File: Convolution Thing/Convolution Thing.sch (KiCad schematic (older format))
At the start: 4 parts, among them U1 Compute_Module_4_Functional

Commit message: Just EE things
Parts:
- removed U1: Compute_Module_4_Functional, CM4:Raspberry-Pi-4-Compute-Module, symbol CM4:Compute_Module_4_Functional
- removed U? (x3): Compute_Module_4_Functional, symbol CM4:Compute_Module_4_Functional
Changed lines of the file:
@@
 $Descr A4 11693 8268
 encoding utf-8
-Sheet 1 2
+Sheet 1 4
 Title ""
 Date ""
@@
 Comment4 ""
 $EndDescr
-$Comp
-L CM4:Compute_Module_4_Functional U1
-U 1 1 6100CB94
-P 1100 1150
-F 0 "U1" H 1950 1447 60  0000 C CNN
-F 1 "Compute_Module_4_Functional" H 1950 1341 60  0000 C CNN
-F 2 "CM4:Raspberry-Pi-4-Compute-Module" H 1300 1200 60  0001 L CNN
-F 3 "" H 1300 1000 60  0001 L CNN
-	1    1100 1150
-	1    0    0    -1
-$EndComp
-$Comp
-L CM4:Compute_Module_4_Functional U?
-U 2 1 61012F62
-P 3700 2200
-F 0 "U?" H 4400 2487 60  0000 C CNN
-F 1 "Compute_Module_4_Functional" H 4400 2381 60  0000 C CNN
-F 2 "" H 3900 2250 60  0001 L CNN
-F 3 "" H 3900 2050 60  0001 L CNN
-	2    3700 2200
-	1    0    0    -1
-$EndComp
-$Comp
-L CM4:Compute_Module_4_Functional U?
-U 8 1 61015F4E
-P 1500 2450
-F 0 "U?" H 2108 2737 60  0000 C CNN
-F 1 "Compute_Module_4_Functional" H 2108 2631 60  0000 C CNN
-F 2 "" H 1700 2500 60  0001 L CNN
-F 3 "" H 1700 2300 60  0001 L CNN
-	8    1500 2450
-	1    0    0    -1
-$EndComp
-$Comp
-L CM4:Compute_Module_4_Functional U?
-U 10 1 61019A69
-P 5850 1200
-F 0 "U?" H 6800 1487 60  0000 C CNN
-F 1 "Compute_Module_4_Functional" H 6800 1381 60  0000 C CNN
-F 2 "" H 6050 1250 60  0001 L CNN
-F 3 "" H 6050 1050 60  0001 L CNN
-	10   5850 1200
-	1    0    0    -1
-$EndComp
 $Sheet
-S 2700 5250 800  750
+S 1750 850  800  750
+U 61029798
+F0 "CODEC" 50
+F1 "CODEC.sch" 50
+$EndSheet
+$Sheet
+S 800  850  800  750
 U 61006232
 F0 "PSU" 50
 F1 "PSU.sch" 50
 $EndSheet
+$Sheet
+S 2700 850  850  750
+U 6108AFC4
+F0 "Misc" 50
+F1 "Misc.sch" 50
+$EndSheet
 $EndSCHEMATC

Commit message: Convolution Thing PCB design continues
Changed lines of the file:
@@
 $Descr A4 11693 8268
 encoding utf-8
-Sheet 1 4
+Sheet 1 7
 Title ""
 Date ""
@@
 S 2700 850  850  750
 U 6108AFC4
-F0 "Misc" 50
-F1 "Misc.sch" 50
+F0 "CM4 Misc" 50
+F1 "CM4 Misc.sch" 50
+$EndSheet
+$Sheet
+S 3700 850  850  750
+U 610884FE
+F0 "CM4 GPIO" 50
+F1 "CM4 GPIO.sch" 50
+$EndSheet
+$Sheet
+S 5700 850  850  750
+U 610554DD
+F0 "Audio Out" 50
+F1 "Audio Out.sch" 50
+$EndSheet
+$Sheet
+S 4700 850  850  750
+U 61055545
+F0 "Audio In" 50
+F1 "Audio In.sch" 50
 $EndSheet
 $EndSCHEMATC

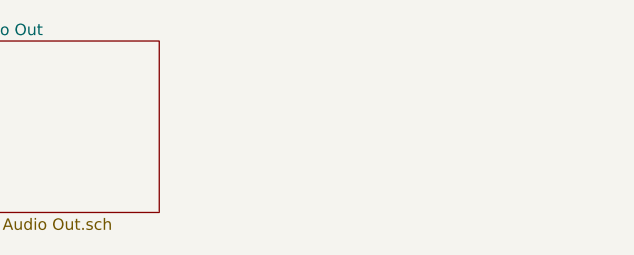
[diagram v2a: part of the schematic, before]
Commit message: Audio I/O, CV input, GPIO work & misc changes
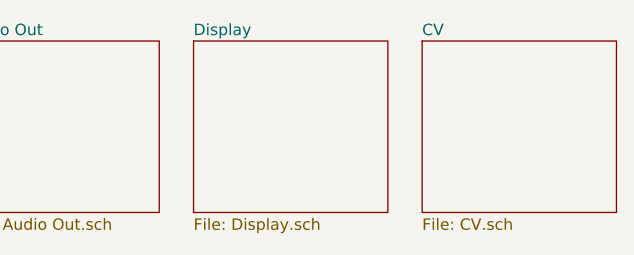
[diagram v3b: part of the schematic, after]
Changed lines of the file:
@@
 $Descr A4 11693 8268
 encoding utf-8
-Sheet 1 7
+Sheet 1 9
 Title ""
 Date ""
@@
 F1 "Audio In.sch" 50
 $EndSheet
+$Sheet
+S 6700 850  850  750
+U 6110E798
+F0 "Display" 50
+F1 "Display.sch" 50
+$EndSheet
+$Sheet
+S 7700 850  850  750
+U 611124FC
+F0 "CV" 50
+F1 "CV.sch" 50
+$EndSheet
 $EndSCHEMATC

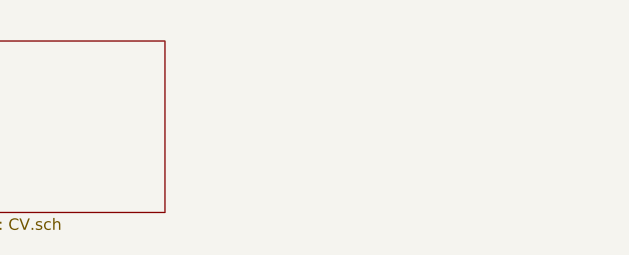
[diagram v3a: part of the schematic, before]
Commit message: Better CV inputs, LED driver, display & USB interfaces
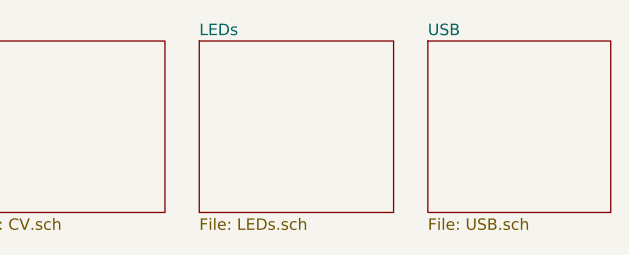
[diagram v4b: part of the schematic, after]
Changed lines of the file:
@@
 $Descr A4 11693 8268
 encoding utf-8
-Sheet 1 9
+Sheet 1 11
 Title ""
 Date ""
@@
 F1 "CV.sch" 50
 $EndSheet
+$Sheet
+S 8700 850  850  750
+U 611DE4E7
+F0 "LEDs" 50
+F1 "LEDs.sch" 50
+$EndSheet
+$Sheet
+S 9700 850  800  750
+U 61201209
+F0 "USB" 50
+F1 "USB.sch" 50
+$EndSheet
 $EndSCHEMATC

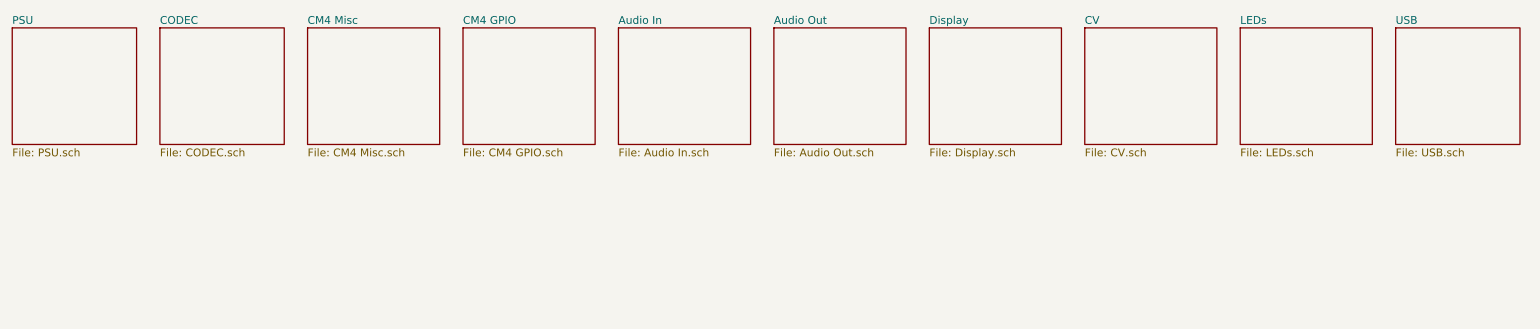
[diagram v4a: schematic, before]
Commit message: Added gate inputs and CM4 / display sockets, made CV inputs 100k, lots of smaller changes. First iteration of schematic now done.
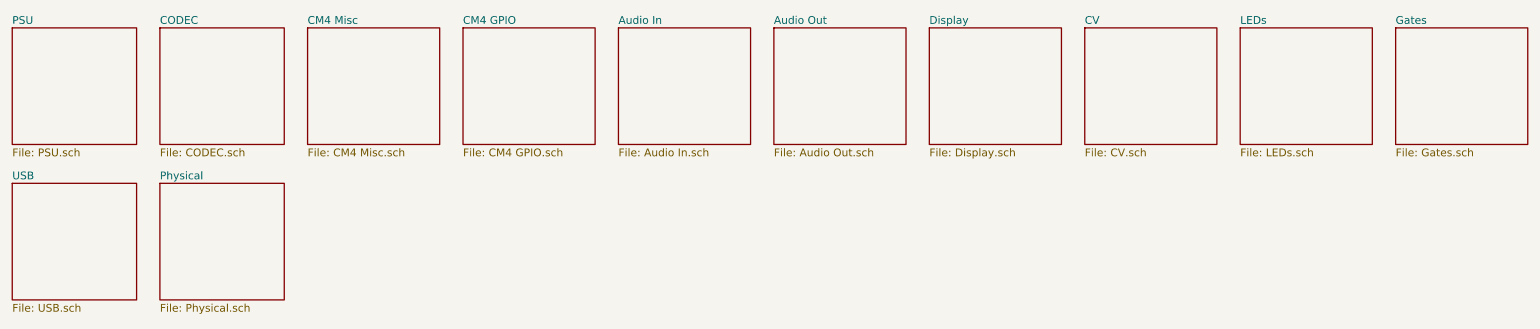
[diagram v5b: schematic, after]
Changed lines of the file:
@@
 $Descr A4 11693 8268
 encoding utf-8
-Sheet 1 11
+Sheet 1 13
 Title ""
 Date ""
@@
 $EndSheet
 $Sheet
-S 9700 850  800  750
+S 800  1850 800  750
 U 61201209
 F0 "USB" 50
 F1 "USB.sch" 50
 $EndSheet
+$Sheet
+S 9700 850  850  750
+U 610C04CE
+F0 "Gates" 50
+F1 "Gates.sch" 50
+$EndSheet
+$Sheet
+S 1750 1850 800  750
+U 610E9296
+F0 "Physical" 50
+F1 "Physical.sch" 50
+$EndSheet
 $EndSCHEMATC

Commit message: PCB layout work and related changes to the schematic
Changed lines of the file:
@@
 $EndDescr
 $Sheet
-S 1750 850  800  750
+S 2700 850  850  750
 U 61029798
 F0 "CODEC" 50
@@
 $EndSheet
 $Sheet
-S 2700 850  850  750
-U 6108AFC4
-F0 "CM4 Misc" 50
-F1 "CM4 Misc.sch" 50
-$EndSheet
-$Sheet
 S 3700 850  850  750
 U 610884FE
-F0 "CM4 GPIO" 50
-F1 "CM4 GPIO.sch" 50
+F0 "GPIO" 50
+F1 "GPIO.sch" 50
 $EndSheet
 $Sheet
@@
 F1 "Physical.sch" 50
 $EndSheet
+$Sheet
+S 1750 850  850  750
+U 6121D935
+F0 "CM4" 50
+F1 "CM4.sch" 50
+$EndSheet
 $EndSCHEMATC

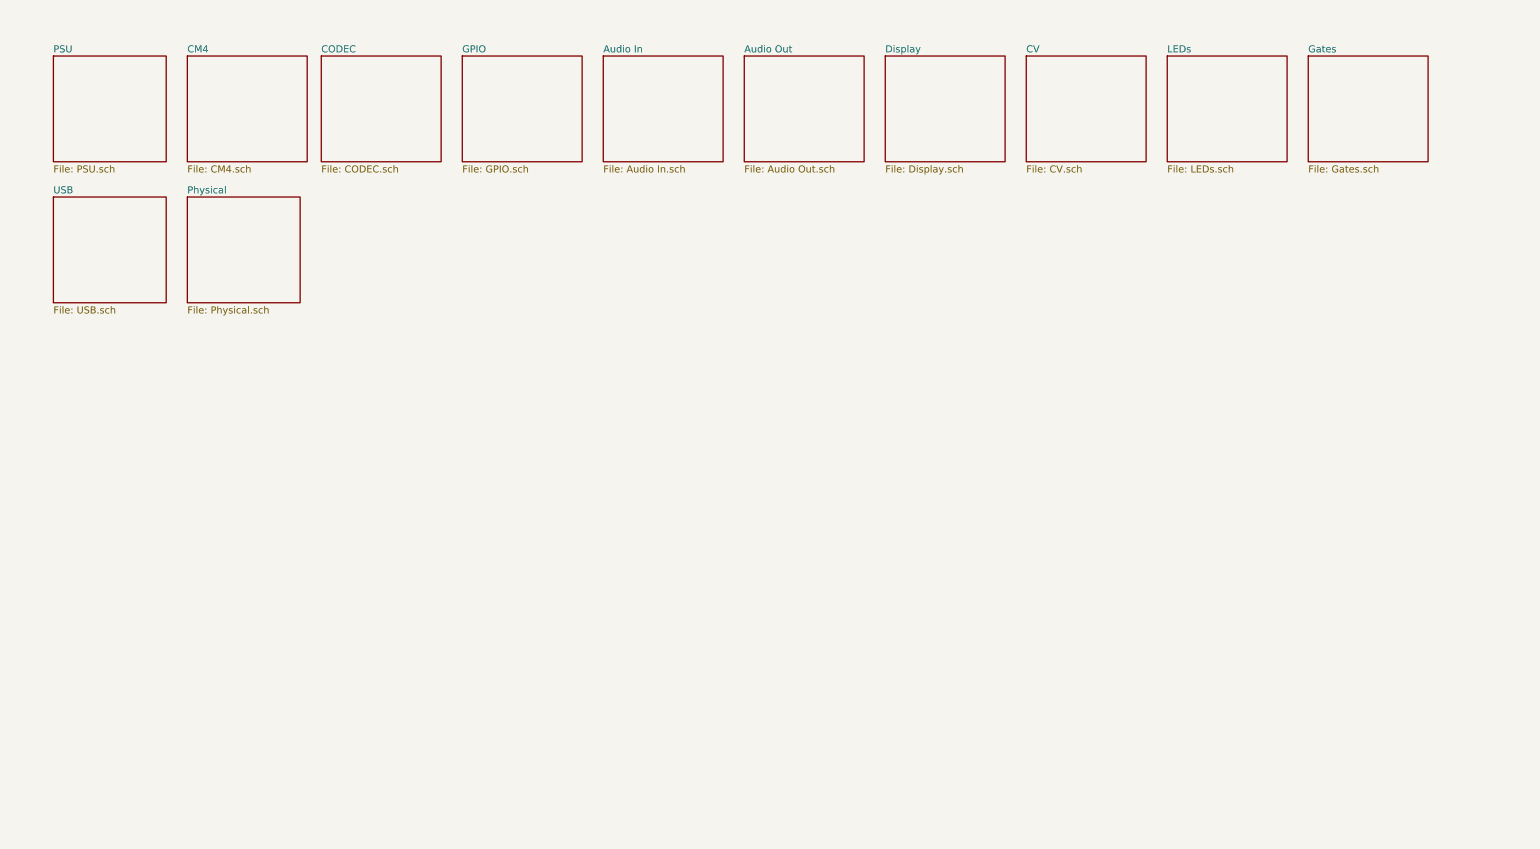
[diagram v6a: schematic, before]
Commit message: Entirely new, simpler PCB
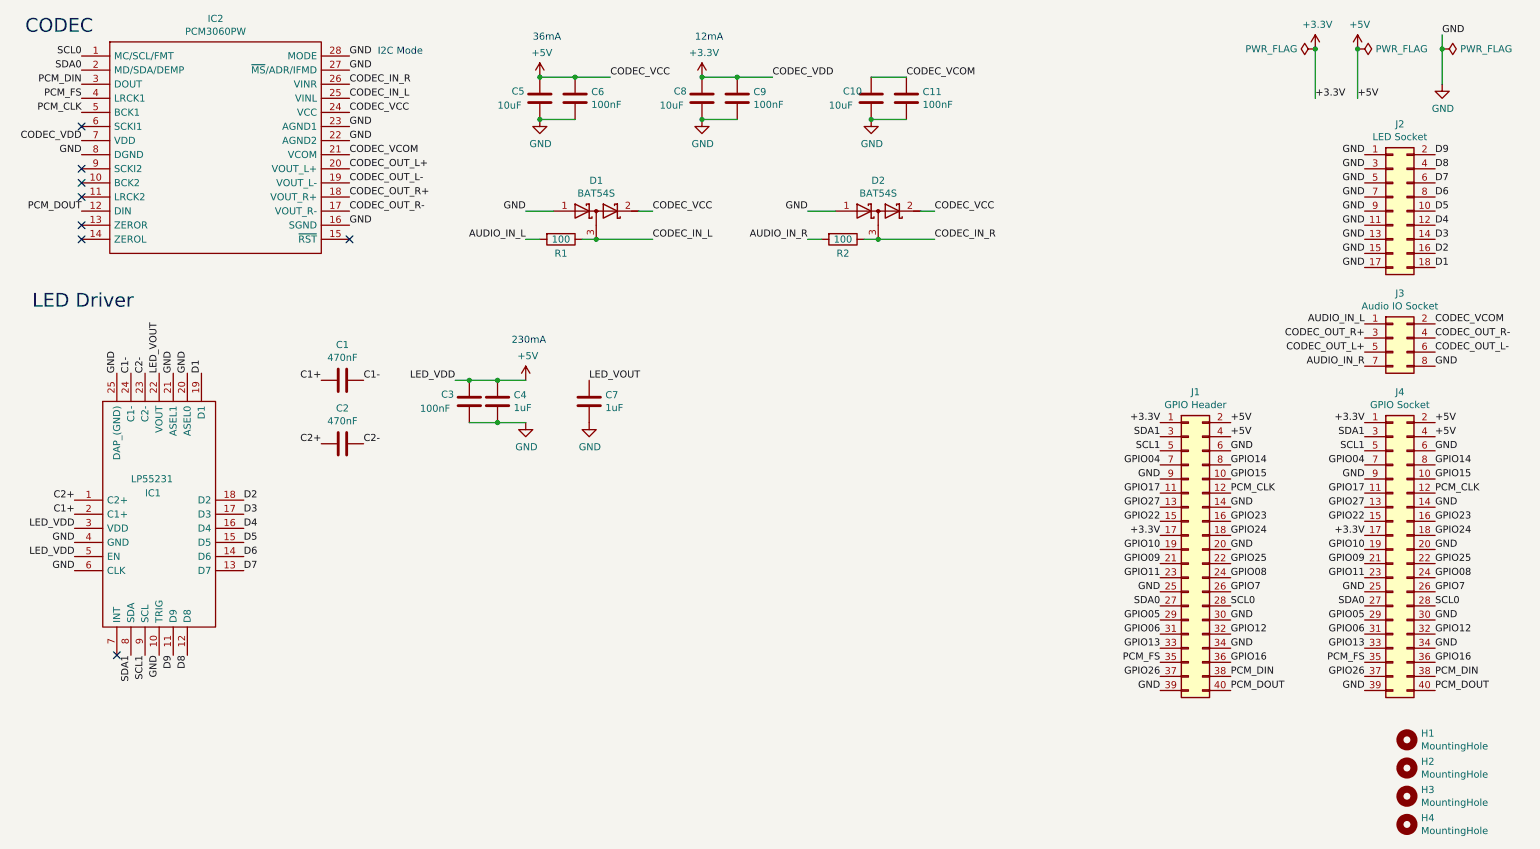
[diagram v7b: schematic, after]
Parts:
- added C1, C2: 470nF, Capacitor_THT:C_Rect_L4.6mm_W3.0mm_P2.50mm_MKS02_FKP02, symbol Device:C
- added C10, C5, C8: 10uF, Capacitor_THT:C_Rect_L4.6mm_W3.0mm_P2.50mm_MKS02_FKP02, symbol Device:C
- added C11, C3, C6, C9: 100nF, Capacitor_THT:C_Rect_L4.6mm_W3.0mm_P2.50mm_MKS02_FKP02, symbol Device:C
- added C4, C7: 1uF, Capacitor_THT:C_Rect_L4.6mm_W3.0mm_P2.50mm_MKS02_FKP02, symbol Device:C
- added D1, D2: BAT54S, Package_TO_SOT_SMD:SOT-323_SC-70_Handsoldering, symbol Device:D_Schottky_x2_Serial_AKC
- added H1, H2, H3, H4: MountingHole, Omat:MountingHole_2.75mm_M2.5, symbol Mechanical:MountingHole
- added IC1: LP55231, SamacSys:QFN50P400X400X80-25N, symbol SamacSys:LP55231SQE_NOPB
- added IC2: PCM3060PW, SamacSys:SOP65P640X120-28N, symbol SamacSys:PCM3060PW
- added J1: GPIO Header, Connector_PinHeader_2.54mm:PinHeader_2x20_P2.54mm_Vertical, symbol Connector_Generic:Conn_02x20_Odd_Even
- added J2: LED Socket, Connector_PinSocket_2.54mm:PinSocket_2x09_P2.54mm_Vertical, symbol Connector_Generic:Conn_02x09_Odd_Even
- added J3: Audio IO Socket, Connector_PinSocket_2.54mm:PinSocket_2x04_P2.54mm_Vertical, symbol Connector_Generic:Conn_02x04_Odd_Even
- added J4: GPIO Socket, Connector_PinSocket_2.54mm:PinSocket_2x20_P2.54mm_Vertical, symbol Connector_Generic:Conn_02x20_Odd_Even
- added R1, R2: 100, Resistor_THT:R_Axial_DIN0207_L6.3mm_D2.5mm_P10.16mm_Horizontal, symbol Device:R
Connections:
- new net +3V3: C8.1, C9.1, IC2.7 (VDD), J1.1 (Pin_1), J1.17 (Pin_17), J4.1 (Pin_1), J4.17 (Pin_17)
- new net +5V: C3.1, C4.1, C5.1, C6.1, D1.2 (K), D2.2 (K), IC1.3 (VDD), IC1.5 (EN), IC2.24 (VCC), J1.2 (Pin_2), J1.4 (Pin_4), J4.2 (Pin_2), J4.4 (Pin_4)
- new net AUDIO_IN_L: J3.1 (Pin_1), R1.2
- new net AUDIO_IN_R: J3.7 (Pin_7), R2.2
- new net C1+: C1.2, IC1.2 (C1+)
- new net C1-: C1.1, IC1.24 (C1-)
- new net C2+: C2.2, IC1.1 (C2+)
- new net C2-: C2.1, IC1.23 (C2-)
- new net CODEC_IN_L: D1.3 (common), IC2.25 (VINL), R1.1
- new net CODEC_IN_R: D2.3 (common), IC2.26 (VINR), R2.1
- new net CODEC_OUT_L+: IC2.20 (VOUT_L+), J3.5 (Pin_5)
- new net CODEC_OUT_L-: IC2.19 (VOUT_L-), J3.6 (Pin_6)
- new net CODEC_OUT_R+: IC2.18 (VOUT_R+), J3.3 (Pin_3)
- new net CODEC_OUT_R-: IC2.17 (VOUT_R-), J3.4 (Pin_4)
- new net CODEC_VCOM: C10.1, C11.1, IC2.21 (VCOM), J3.2 (Pin_2)
- new net D1: IC1.19 (D1), J2.18 (Pin_18)
- new net D2: IC1.18 (D2), J2.16 (Pin_16)
- new net D3: IC1.17 (D3), J2.14 (Pin_14)
- new net D4: IC1.16 (D4), J2.12 (Pin_12)
- new net D5: IC1.15 (D5), J2.10 (Pin_10)
- new net D6: IC1.14 (D6), J2.8 (Pin_8)
- new net D7: IC1.13 (D7), J2.6 (Pin_6)
- new net D8: IC1.12 (D8), J2.4 (Pin_4)
- new net D9: IC1.11 (D9), J2.2 (Pin_2)
- new net GND: C10.2, C11.2, C3.2, C4.2, C5.2, C6.2, C7.2, C8.2, C9.2, D1.1 (A), D2.1 (A), IC1.10 (TRIG), IC1.20 (ASEL0), IC1.21 (ASEL1), IC1.25 (DAP_(GND)), IC1.4 (GND), IC1.6 (CLK), IC2.16 (SGND), IC2.22 (AGND2), IC2.23 (AGND1), IC2.27 (~MS~/ADR/IFMD), IC2.28 (MODE), IC2.8 (DGND), J1.14 (Pin_14), J1.20 (Pin_20), J1.25 (Pin_25), J1.30 (Pin_30), J1.34 (Pin_34), J1.39 (Pin_39), J1.6 (Pin_6), J1.9 (Pin_9), J2.1 (Pin_1), J2.11 (Pin_11), J2.13 (Pin_13), J2.15 (Pin_15), J2.17 (Pin_17), J2.3 (Pin_3), J2.5 (Pin_5), J2.7 (Pin_7), J2.9 (Pin_9), J3.8 (Pin_8), J4.14 (Pin_14), J4.20 (Pin_20), J4.25 (Pin_25), J4.30 (Pin_30), J4.34 (Pin_34), J4.39 (Pin_39), J4.6 (Pin_6), J4.9 (Pin_9)
- new net GPIO04: J1.7 (Pin_7), J4.7 (Pin_7)
- new net GPIO05: J1.29 (Pin_29), J4.29 (Pin_29)
- new net GPIO06: J1.31 (Pin_31), J4.31 (Pin_31)
- new net GPIO08: J1.24 (Pin_24), J4.24 (Pin_24)
- new net GPIO09: J1.21 (Pin_21), J4.21 (Pin_21)
- new net GPIO10: J1.19 (Pin_19), J4.19 (Pin_19)
- new net GPIO11: J1.23 (Pin_23), J4.23 (Pin_23)
- new net GPIO12: J1.32 (Pin_32), J4.32 (Pin_32)
- new net GPIO13: J1.33 (Pin_33), J4.33 (Pin_33)
- new net GPIO14: J1.8 (Pin_8), J4.8 (Pin_8)
- new net GPIO15: J1.10 (Pin_10), J4.10 (Pin_10)
- new net GPIO16: J1.36 (Pin_36), J4.36 (Pin_36)
- new net GPIO17: J1.11 (Pin_11), J4.11 (Pin_11)
- new net GPIO22: J1.15 (Pin_15), J4.15 (Pin_15)
- new net GPIO23: J1.16 (Pin_16), J4.16 (Pin_16)
- new net GPIO24: J1.18 (Pin_18), J4.18 (Pin_18)
- new net GPIO25: J1.22 (Pin_22), J4.22 (Pin_22)
- new net GPIO26: J1.37 (Pin_37), J4.37 (Pin_37)
- new net GPIO27: J1.13 (Pin_13), J4.13 (Pin_13)
- new net GPIO7: J1.26 (Pin_26), J4.26 (Pin_26)
- new net LED_VOUT: C7.1, IC1.22 (VOUT)
- new net PCM_CLK: IC2.5 (BCK1), J1.12 (Pin_12), J4.12 (Pin_12)
- new net PCM_DIN: IC2.3 (DOUT), J1.38 (Pin_38), J4.38 (Pin_38)
- new net PCM_DOUT: IC2.12 (DIN), J1.40 (Pin_40), J4.40 (Pin_40)
- new net PCM_FS: IC2.4 (LRCK1), J1.35 (Pin_35), J4.35 (Pin_35)
- new net SCL0: IC2.1 (MC/SCL/FMT), J1.28 (Pin_28), J4.28 (Pin_28)
- new net SCL1: IC1.9 (SCL), J1.5 (Pin_5), J4.5 (Pin_5)
- new net SDA0: IC2.2 (MD/SDA/DEMP), J1.27 (Pin_27), J4.27 (Pin_27)
- new net SDA1: IC1.8 (SDA), J1.3 (Pin_3), J4.3 (Pin_3)
- no-connect marks 0 -> 8
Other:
- note added: "12mA"
- note added: "230mA"
- note added: "36mA"
- note added: "CODEC"
- note added: "I2C Mode"
- note added: "LED Driver"
